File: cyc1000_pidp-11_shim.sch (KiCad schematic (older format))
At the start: 16 parts, among them J1 FTDI_FRIEND, J11 Raspberry_Hat, J12 RS232_PMOD, J13 USD_PMOD, J14 ETH_PMOD, J4 POWER, U1 CYC1000

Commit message: Generate gerbers
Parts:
- removed C2: 270u, Capacitor_THT:CP_Radial_D8.0mm_P3.50mm, symbol Device:CP1
- removed C3: 0.1, Capacitor_SMD:C_0603_1608Metric_Pad1.08x0.95mm_HandSolder, symbol Device:C
- removed C7: 10u, Capacitor_SMD:C_0603_1608Metric_Pad1.08x0.95mm_HandSolder, symbol Device:C
- added C4: 0.1, Capacitor_THT:C_Disc_D5.0mm_W2.5mm_P5.00mm, symbol Device:C
- C5: value 10u -> 0.1; footprint Capacitor_SMD:C_0603_1608Metric_Pad1.08x0.95mm_HandSolder -> Capacitor_THT:C_Disc_D5.0mm_W2.5mm_P5.00mm
- renumbered C4 to C2, C6 to C3, C8 to C6
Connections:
- net GND: now also C4.2
- net VCC33: now also C4.1
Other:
- note added: "All capacitors are optional, but recommended."
- note added: "RTS/CTS are not currently implemented in the FPGA."
- note added: "You can either use a Digilent RS232 PMOD or an\nAdaFruit FTDI-Friend, but not both at the same\ntime."
- note removed: "All capacitors are optional."
- note removed: "RTS/CTS not currently implemented in FPGA."
- note removed: "You can either use a Digilent RS232 PMOD or an\nAdaFruit FTDI-Friend."
- moved on the sheet: C1, C2, C3, C6, J4

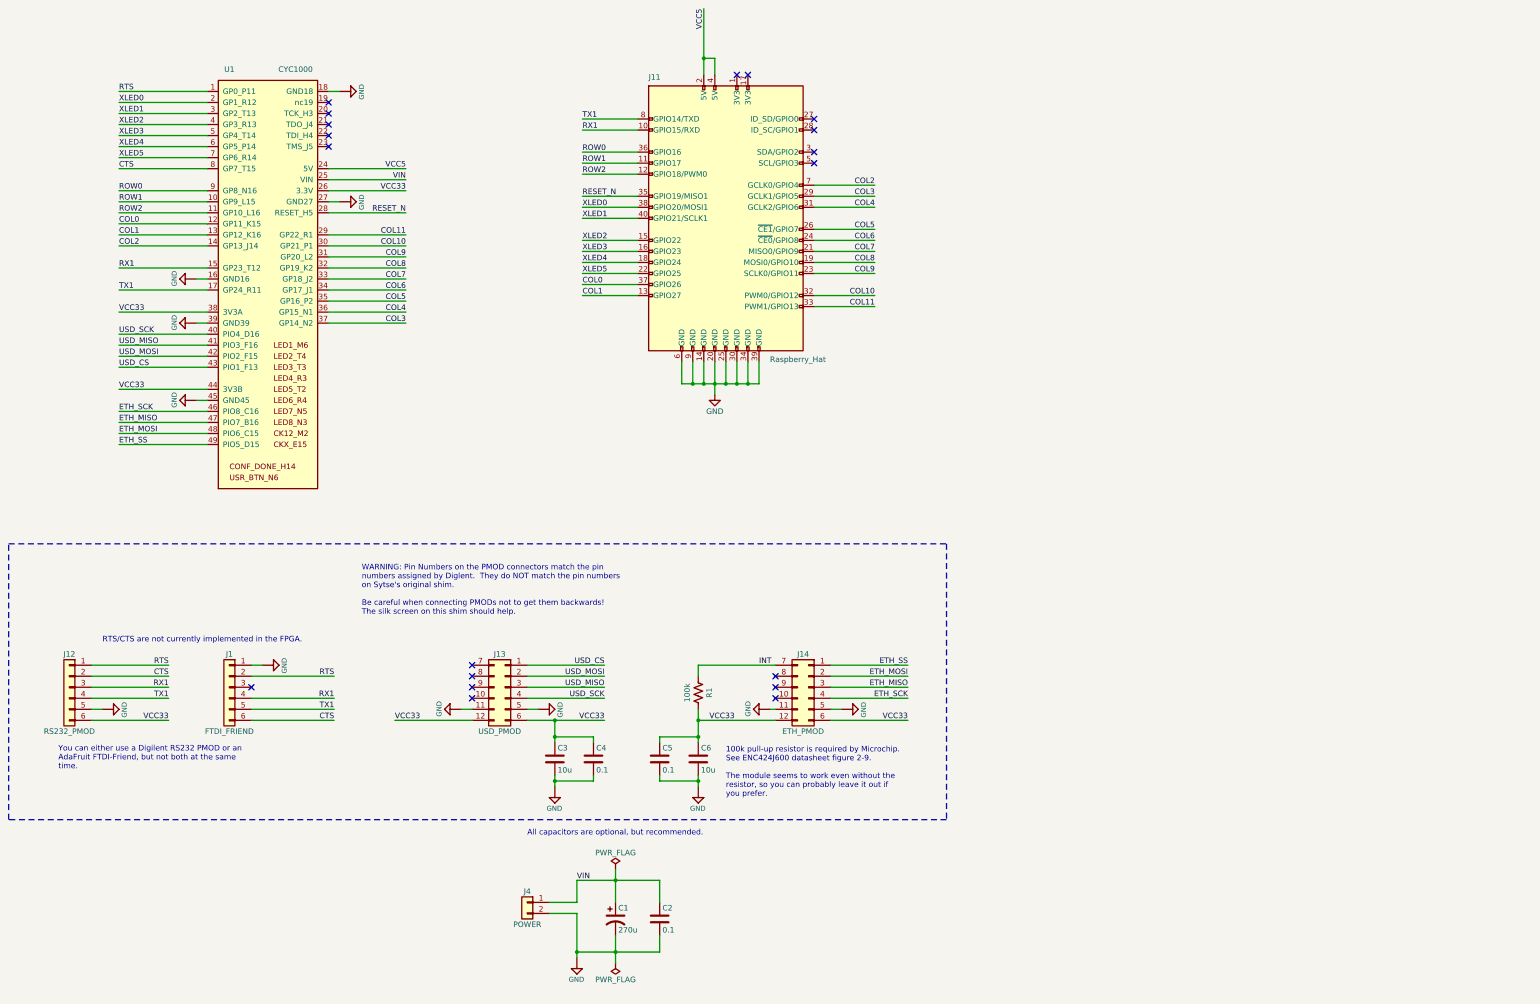
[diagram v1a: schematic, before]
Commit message: Remove extra caps, add comments
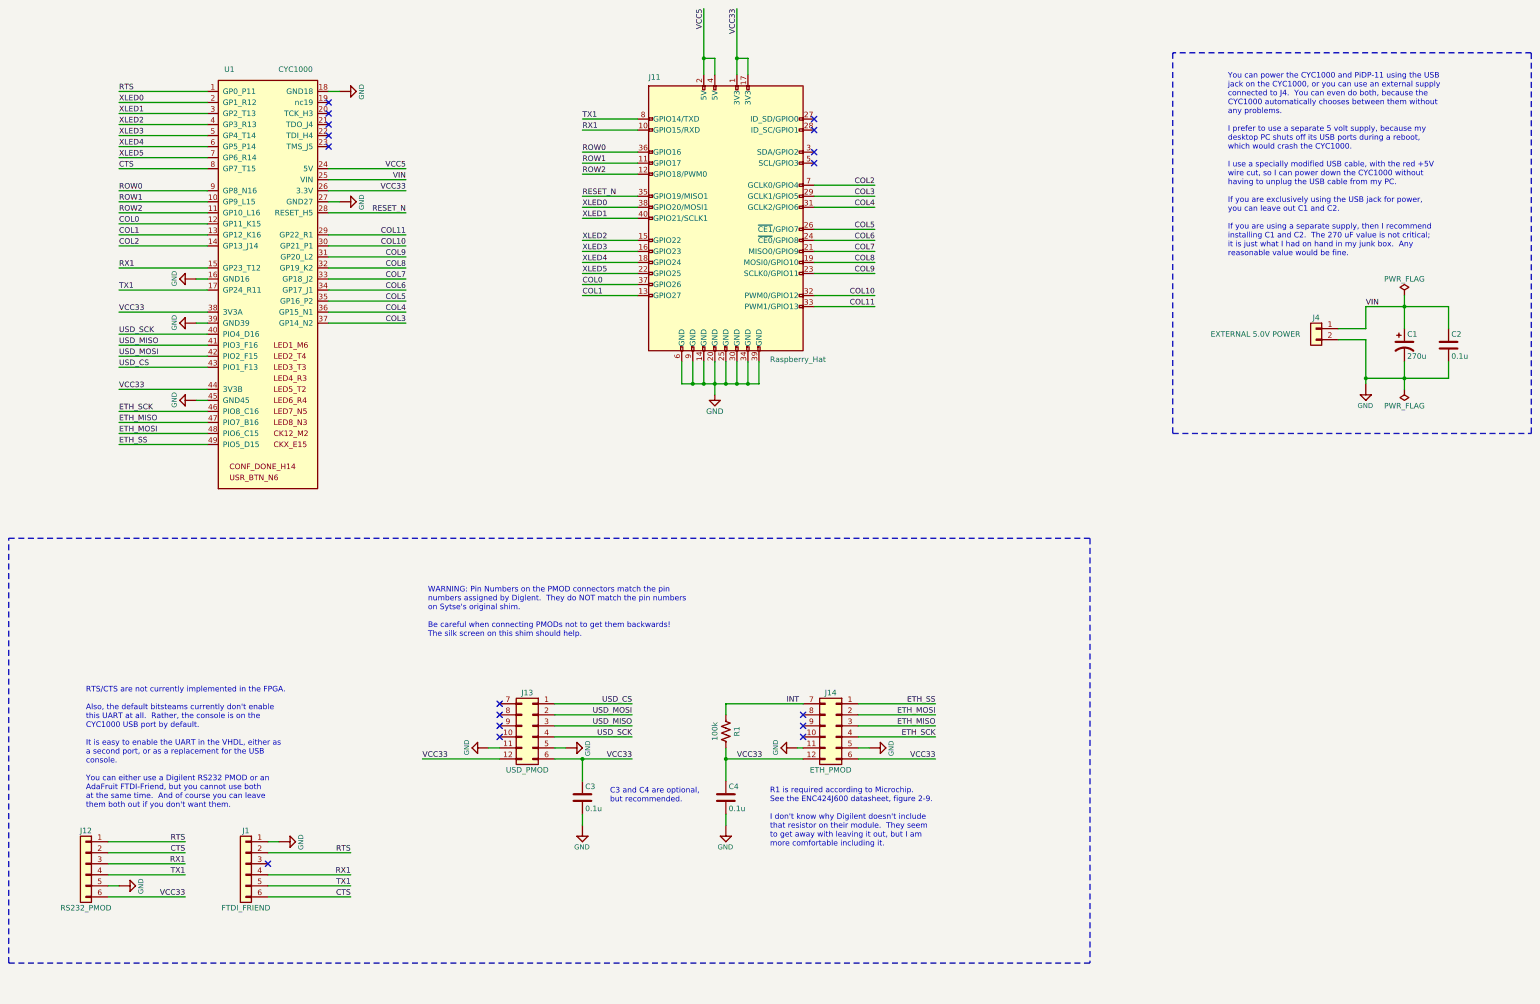
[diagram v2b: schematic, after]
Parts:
- removed C4, C5: 0.1, Capacitor_THT:C_Disc_D5.0mm_W2.5mm_P5.00mm, symbol Device:C
- C2: value 0.1 -> 0.1u
- C3: value 10u -> 0.1u
- C4: renamed from C6; value 10u -> 0.1u
- J4: value POWER -> EXTERNAL 5.0V POWER
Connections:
- net VCC33: now also J11.1 (3V3), J11.17 (3V3)
- no-connect marks 19 -> 17
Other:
- note added: "C3 and C4 are optional,\nbut recommended."
- note added: "R1 is required according to Microchip.\nSee the ENC424J600 datasheet, figure 2-9.\n\nI don't know why Digilent doesn't include\nthat resistor on their module. They seem\nto get away with leaving it out, but I am\nmore comfortable including it."
- note added: "RTS/CTS are not currently implemented in the FPGA.\n\nAlso, the default bitsteams currently don't enable\nthis UART at all. Rather, the console is on the\nCYC1000 USB port by default.\n\nIt is easy to enable the UART in the VHDL, either as\na second port, or as a replacement for the USB\nconsole.\n\nYou can either use a Digilent RS232 PMOD or an\nAdaFruit FTDI-Friend, but you cannot use both\nat 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"
- note added: "You can power the CYC1000 and PiDP-11 using the USB\njack on the CYC1000, or you can use an external supply\nconnected to J4. You can even do both, because the\nCYC1000 automatically chooses between them without\nany problems.\n\nI prefer to use a separate 5 volt supply, because my\ndesktop PC shuts off its USB ports during a reboot,\nwhich would crash the CYC1000.\n\nI use a specially modified U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"
- note removed: "100k pull-up resistor is required by Microchip.\nSee ENC424J600 datasheet figure 2-9.\n\nThe module seems to work even without the\nresistor, so you can probably leave it out if\nyou prefer."
- note removed: "All capacitors are optional, but recommended."
- note removed: "RTS/CTS are not currently implemented in the FPGA."
- note removed: "You can either use a Digilent RS232 PMOD or an\nAdaFruit FTDI-Friend, but not both at the same\ntime."
- moved on the sheet: C1, C2, C3, C4, J1, J12, J13, J14, J4, R1
